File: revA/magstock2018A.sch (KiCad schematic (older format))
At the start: 37 parts, among them J1 Audio In, J2 5vdcIn, J3 WS2813, J4 WS2813, P1 USBMicroB-10118194-0001LF, SW1 TACTILE, SW2 TACTILE, SW3 TACTILE, SW4 TACTILE, SW5 TACTILE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

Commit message: Update files
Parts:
- removed J4: WS2813, Molex_KK-6410-04_04x2.54mm_Straight, symbol Conn_01x04
- removed R6: 10k, R_0805, symbol R
- removed U3: CP2104, QFN-24-1EP_4x4mm_Pitch0.5mm, symbol CP2104
- added J4: Conn_01x05, symbol Conn_01x05
- added P2: CONN_1, WagonBG, symbol CONN_1
- added P3: CONN_1, HOLE832, symbol CONN_1
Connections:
- net labels added: D+, D-, TUSB
- net labels removed: I2SI
- wire segments 100 -> 102
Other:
- moved on the sheet: D5, D7, ESP1, R2, R3, R5, SW2, SW3, SW4, SW5, SW6, U2

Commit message: Update reva
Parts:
- added R6: 1.5k, R_0805, symbol R
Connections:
- net +3V3: now also R6.1; no longer J4.4 (Pin_4)
- net D+: now also ESP1.20 (GPIO5); no longer P1.2 (D-)
- net VCC: now also J4.4 (Pin_4)
- net at ESP1.18 (GPIO0), R3.2, SW6.1: now also J4.5 (Pin_5)
- net D-: now reaches ESP1.19 (GPIO4)
- net D-: now also P1.2 (D-), R6.2

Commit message: Update to rev b.
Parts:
- removed J1: Audio In, 35RAPC4BH3, symbol Conn_01x05
- added J1: Conn_01x03, 3.5mm_barrel_jack_MJ-3536N, symbol Conn_01x03
- added R7, R8, R9: 4k7, R_0805, symbol R
- J4: footprint (none) -> Molex_KK-6410-05_05x2.54mm_Straight
- R2, R3, R5: value 10k -> 4k7
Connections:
- net +3V3: now also R7.2, R8.2, R9.2
- net GND: now also J1.1 (Pin_1)
- net at ESP1.5 (GPIO14), SW1.1: now also R7.1
- net at ESP1.6 (GPIO12), SW2.1: now also R8.1
- net at ESP1.7 (GPIO13), SW4.1: now also R9.1
- net at C3.1, MK1.2 (+), R4.2: now also J1.3 (Pin_3)
- net at C2.2: now also J1.2 (Pin_2)
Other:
- moved on the sheet: J2

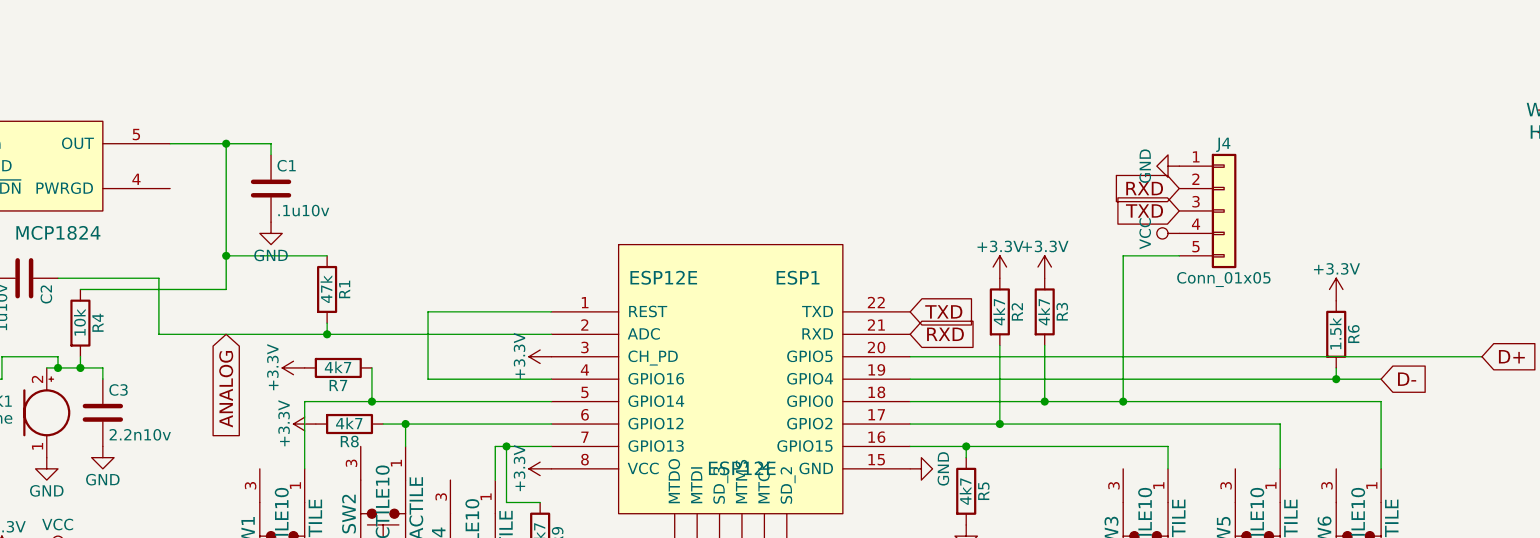
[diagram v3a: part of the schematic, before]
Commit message: Update to optional revc
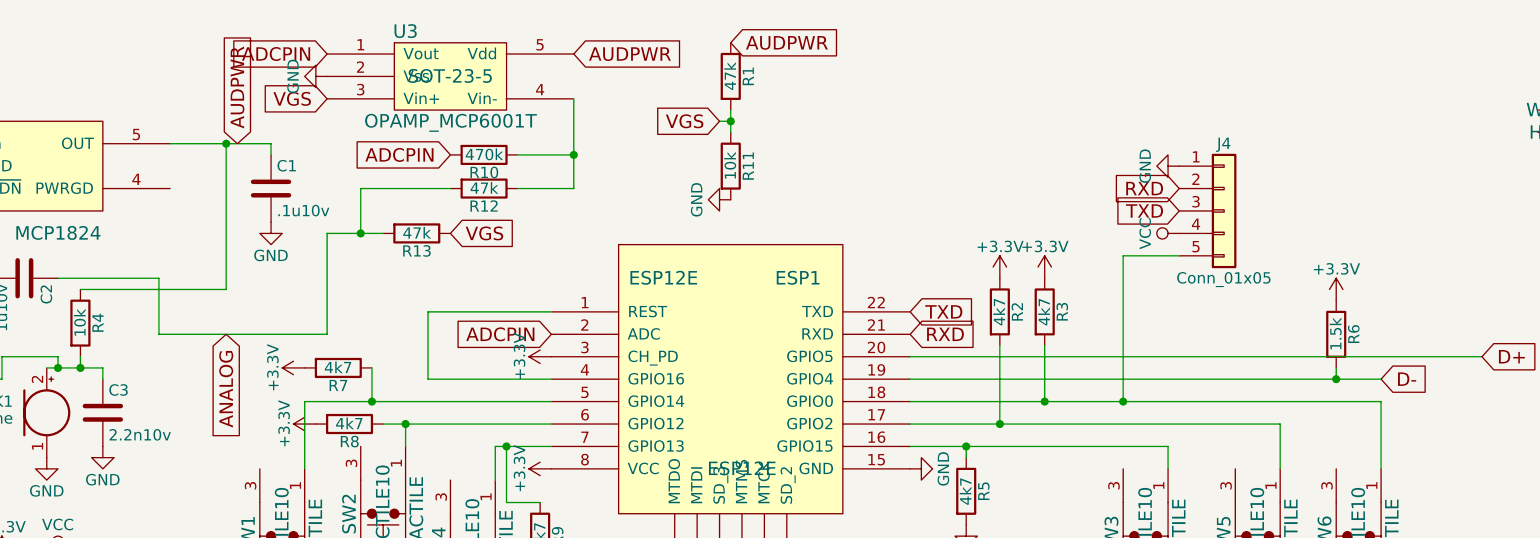
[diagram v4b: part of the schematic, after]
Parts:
- added R10: 470k, R_0805, symbol R
- added R11: 10k, R_0805, symbol R
- added R12, R13: 47k, R_0805, symbol R
- added U3: OPAMP_MCP6001T, SOT-23-5, symbol OPAMP_MCP6001T
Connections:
- net ANALOG: now also R12.2, R13.2; no longer ESP1.2 (ADC), R1.2
- net GND: now also R11.2, U3.2 (Vss)
- net AUDPWR: now reaches C1.1, R1.1, R4.1, U1.5 (OUT)
- net AUDPWR: now also U3.5 (Vdd)
- new net: R10.1, R12.1, U3.4 (Vin-)
- new net ADCPIN: ESP1.2 (ADC), R10.2, U3.1 (Vout)
- new net VGS: R1.2, R11.1, R13.1, U3.3 (Vin+)

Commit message: bump
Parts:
- U1: value MCP1824 -> TLV70036
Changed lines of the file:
@@
 LIBS:switches
 LIBS:relays
+LIBS:motors
 LIBS:transistors
 LIBS:conn
@@
 P 1550 1350
 F 0 "U1" H 1300 1650 60  0000 C CNN
-F 1 "MCP1824" H 1650 1050 60  0000 C CNN
+F 1 "TLV70036" H 1650 1050 60  0000 C CNN
 F 2 "SOT-23-5_HandSoldering" H 1550 1350 60  0001 C CNN
 F 3 "" H 1550 1350 60  0001 C CNN

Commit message: Bump everything
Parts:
- added C7: 10u, R_0805, symbol C
- C3: value 2.2n10v -> NOPOP
- R10: value 470k -> 220k
- R12: value 47k -> 22k
- R7, R8, R9: value 4k7 -> NOPOP
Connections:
- net GND: now also C7.2
- net VGS: now also C7.1

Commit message: push extra wire bridge
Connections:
- net TUSB is gone; now on net VCC: D5.2 (A), P1.1 (VCC)
